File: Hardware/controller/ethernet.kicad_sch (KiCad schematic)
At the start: 21 parts

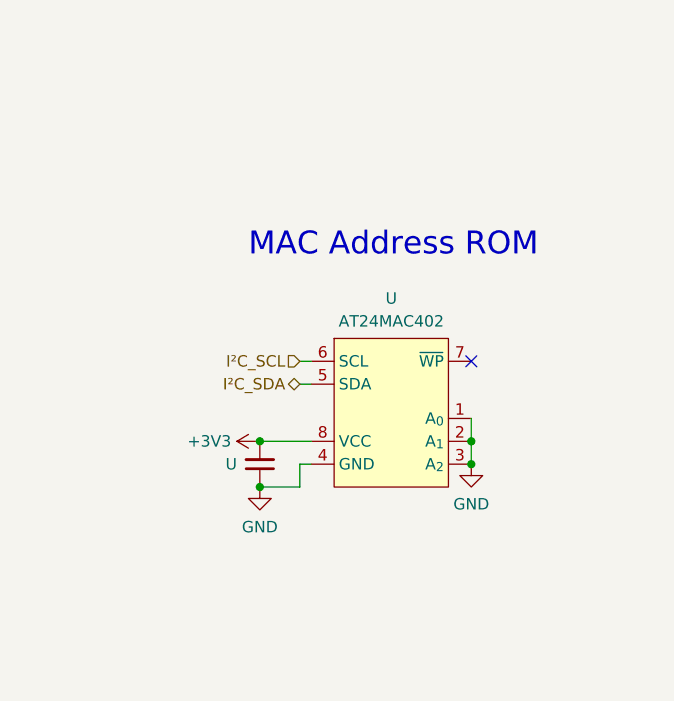
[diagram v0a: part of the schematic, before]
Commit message: Add CAN controller, power switch
- Add the schematic sheet for the CAN bus controller (MCP2515) and
  routed all of its signals, including a CAN transceiver and the
  associated SPI lines for the controller

  (tbh ideally we'd use the CAN inside the STM32 but the STM32MP151 in
  the SoM doesn't have that…)

- Added footprint for the NE1838EE mains power switch and started
  routing part of it

- Various tweaks to controller layout
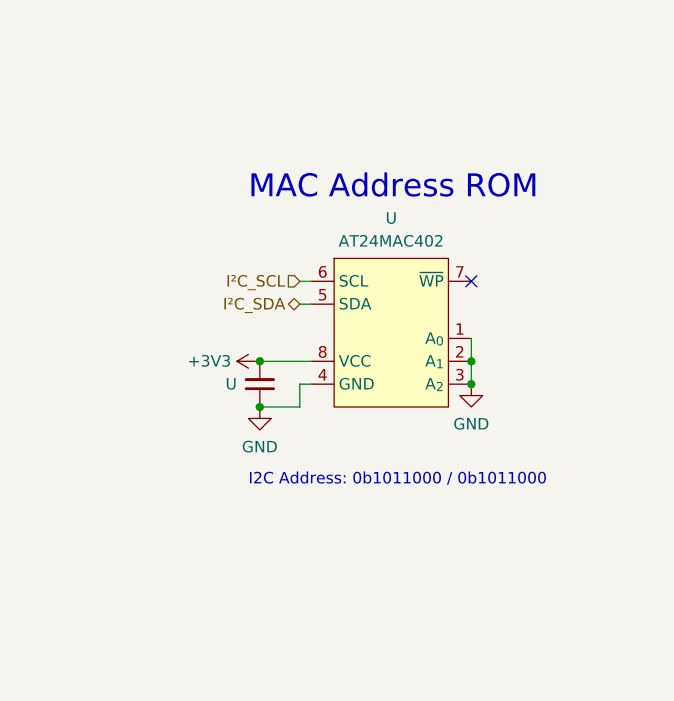
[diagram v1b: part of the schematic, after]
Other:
- note added: "I2C Address: 0b1011000 / 0b1011000"
- moved on the sheet: U

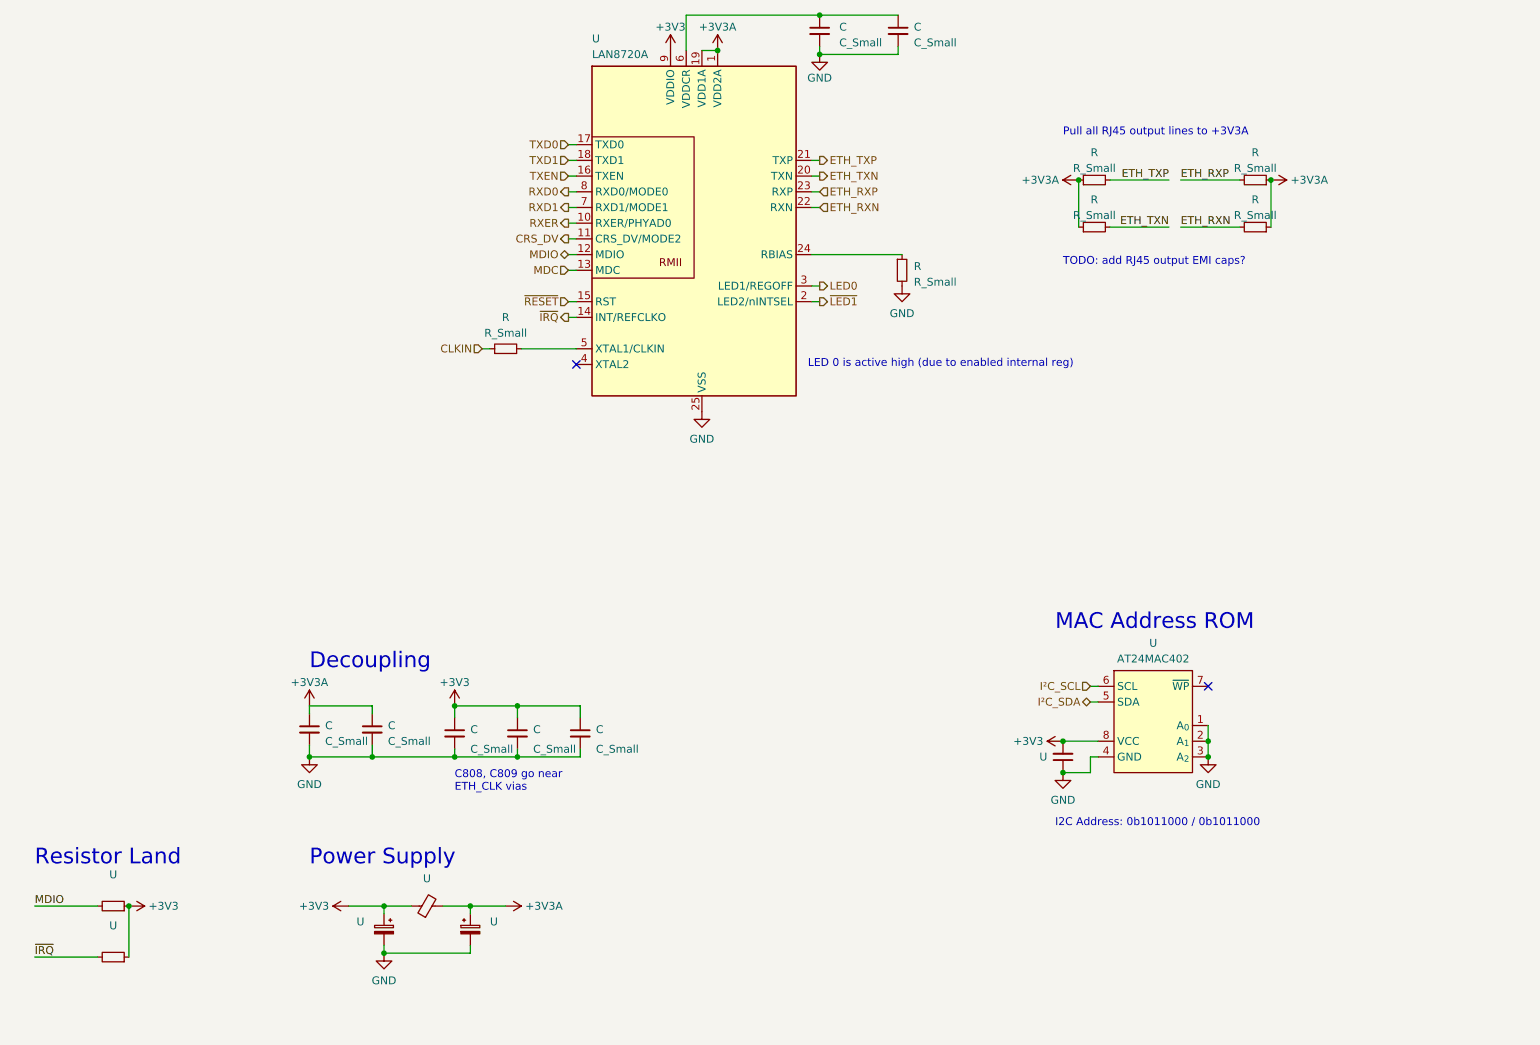
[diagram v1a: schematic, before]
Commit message: Minor Ethernet/IO tweaks
- Added (optional) EMI filter caps to Ethernet diff pairs

- Tweaked routing of the IO section slightly, and routed the GND2 plane
  (chassis ground) which connects to chassis by means of a screw
  terminal "pad" on the bottom right screw

  (Should each screw be conductive? A GND2 ring around the board?)

- Routed CPU SWD connector

- Fixed USB connector footprint to properly break out the shields in a
  way that's compatible with the KiCad USB connector symbols
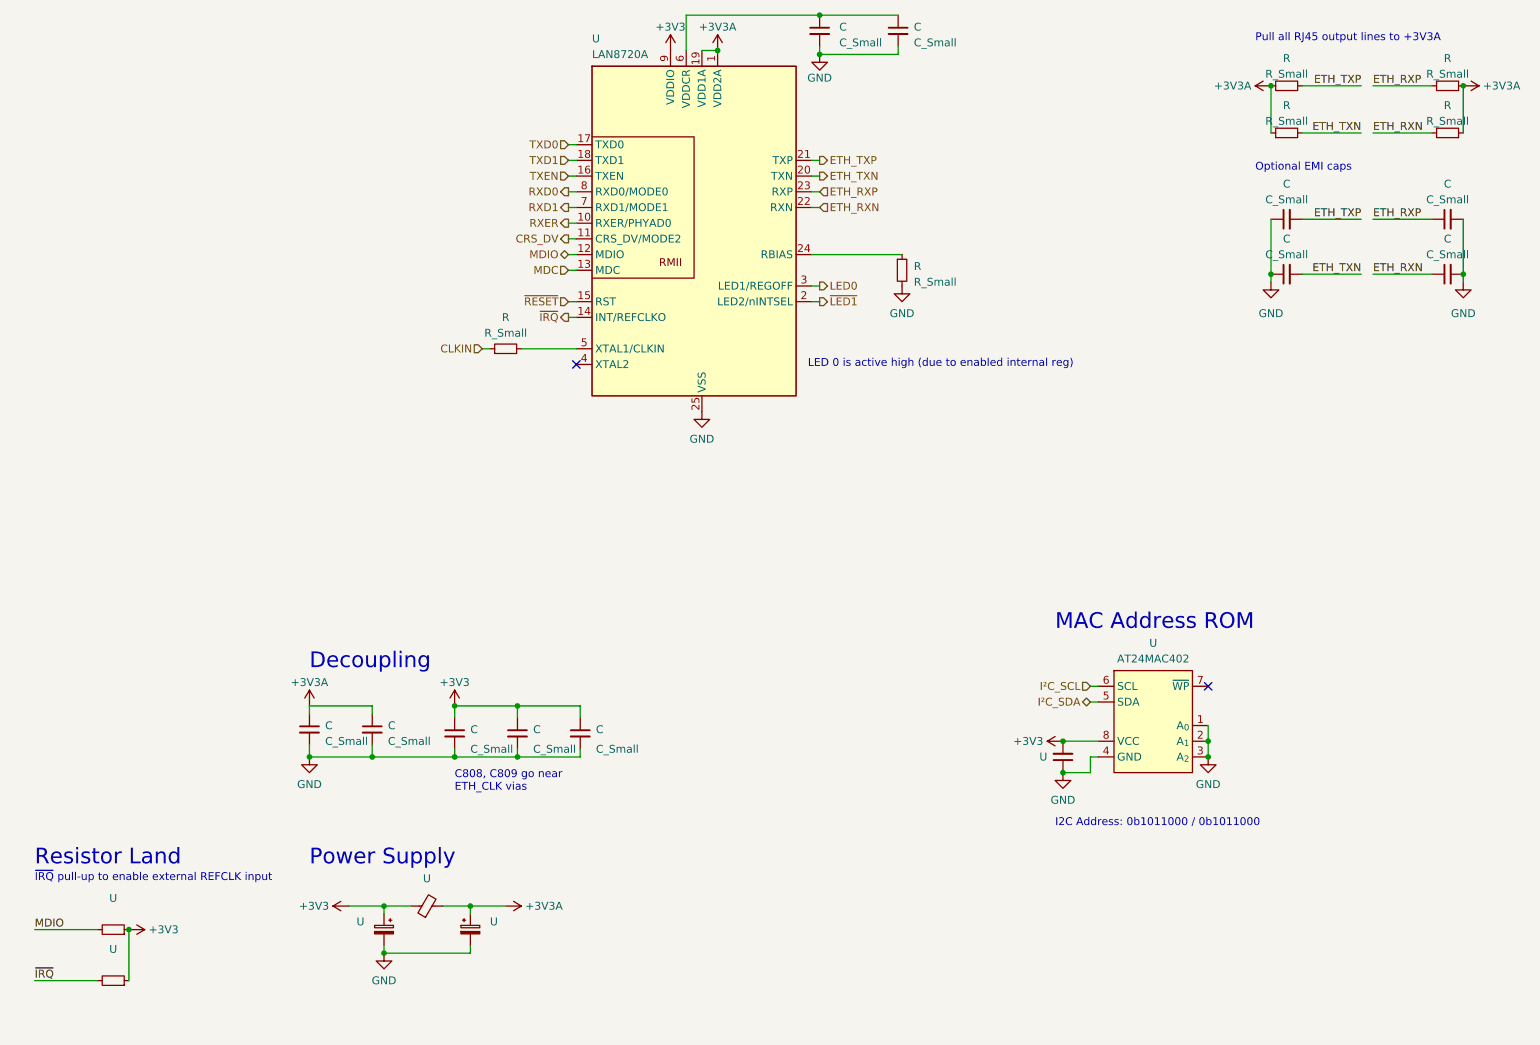
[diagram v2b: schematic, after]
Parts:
- added C (x4): C_Small, symbol Device:C_Small
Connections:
- net ETH_RXN: now also C.1
- net ETH_RXP: now also C.1
- net ETH_TXN: now also C.2
- net ETH_TXP: now also C.2
- net GND: now also C.1, C.1, C.2, C.2
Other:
- note added: "Optional EMI caps"
- note added: "~{IRQ} pull-up to enable external REFCLK input"
- note removed: "TODO: add RJ45 output EMI caps?"
- moved on the sheet: R, U

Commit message: Minor tweaks to front panel & controller for manufacture
- Create footprint for JLCPCB assembly tooling holes

- Added tooling holes to front panel board and fixed ERC errors

- Added tooling holes to controller

- Moved a few traces on controller board and fixed a few broken package
  associations

- Add pull-up on Ethernet PHY's reset line (so when the SoM boots, we're
  not making it angerey)

- Fixed order of BOOTx pins to DIP switch

- Fixed swapped USB host/device pins

- Fixed swapped ETH_TXP/ETH_TXN pair on when exiting the CPU sheet and
  connecting to the rear IO sheet (in the main sheet of the schematic)
  and the associated incorrect resistors/caps
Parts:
- added R: R_Small, symbol Device:R_Small
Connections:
- net +3V3: now also R.2
- net ~{RESET}: now also R.1
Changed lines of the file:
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@@
   (junction (at 75.565 179.07) (diameter 0) (color 0 0 0 0)
+  )
+  (junction (at 34.29 183.515) (diameter 0) (color 0 0 0 0)
   )
   (junction (at 208.915 144.78) (diameter 0) (color 0 0 0 0)
@@
     (stroke (width 0) (type default))
   )
+  (wire (pts (xy 34.29 183.515) (xy 34.29 191.135))
+    (stroke (width 0) (type default))
+  )
   (wire (pts (xy 235.585 38.735) (xy 245.11 38.735))
     (stroke (width 0) (type default))
@@
   )
   (wire (pts (xy 105.41 60.96) (xy 106.68 60.96))
+    (stroke (width 0) (type default))
+  )
+  (wire (pts (xy 19.05 191.135) (xy 29.21 191.135))
     (stroke (width 0) (type default))
   )
@@
   )
   (label "ETH_RXN" (at 235.585 46.355 0) (fields_autoplaced)
+    (effects (font (size 1.27 1.27)) (justify left bottom))
+  )
+  (label "~{RESET}" (at 19.05 191.135 0) (fields_autoplaced)
     (effects (font (size 1.27 1.27)) (justify left bottom))
   )
@@
     (pin "1")
   )
+  (symbol (lib_id "Device:R_Small") (at 31.75 191.135 90) (unit 1)
+    (in_bom yes) (on_board yes)
+    (default_instance (reference "R") (unit 1) (value "R_Small") (footprint ""))
+    (property "Reference" "R" (id 0) (at 31.75 186.69 90)
+      (effects (font (size 1.27 1.27)))
+    )
+    (property "Value" "R_Small" (id 1) (at 31.75 188.595 90)
+      (effects (font (size 1.27 1.27)))
+    )
+    (property "Footprint" "" (id 2) (at 31.75 191.135 0)
+      (effects (font (size 1.27 1.27)) hide)
+    )
+    (property "Datasheet" "~" (id 3) (at 31.75 191.135 0)
+      (effects (font (size 1.27 1.27)) hide)
+    )
+    (pin "1")
+    (pin "2")
+  )
   (symbol (lib_id "programmable-load:+3V3A") (at 95.25 171.45 270) (unit 1)

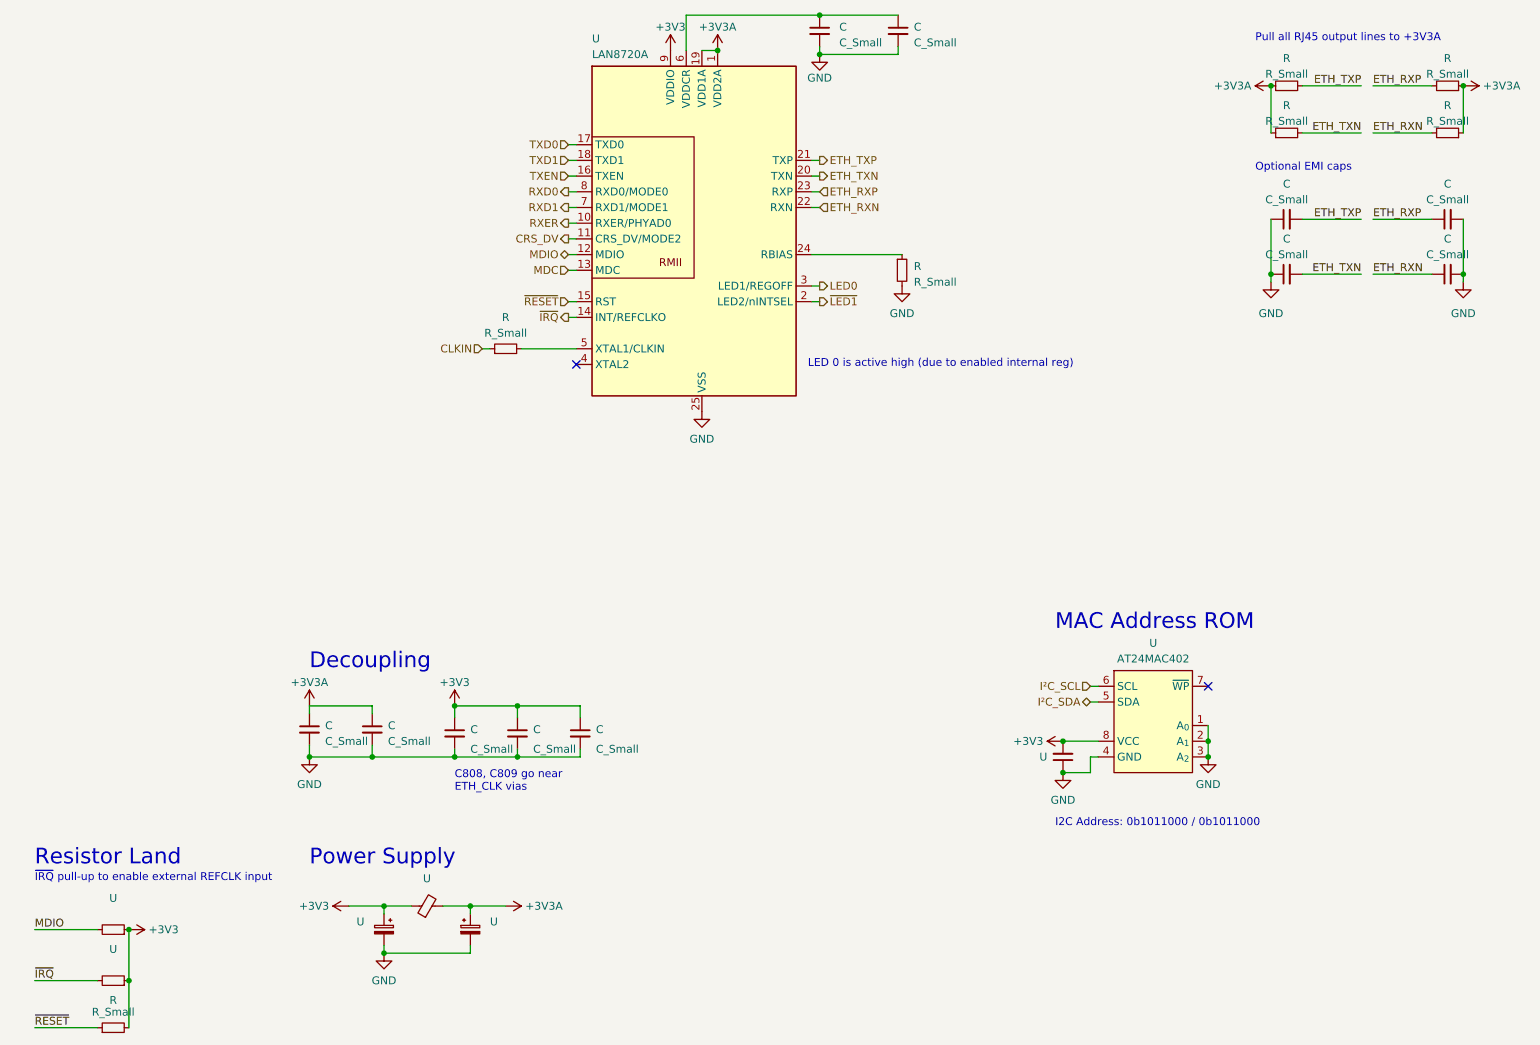
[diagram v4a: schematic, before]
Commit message: Add RMII termination resistors
- Insert resistor networks to terminate the RMII signals both at the MAC
  side and the PHY side, and re-route them with 50Ω impedance.

  Also added some additional resistors to strap pins on boot (for PHY
  address; those for MODE are using the internal ones).
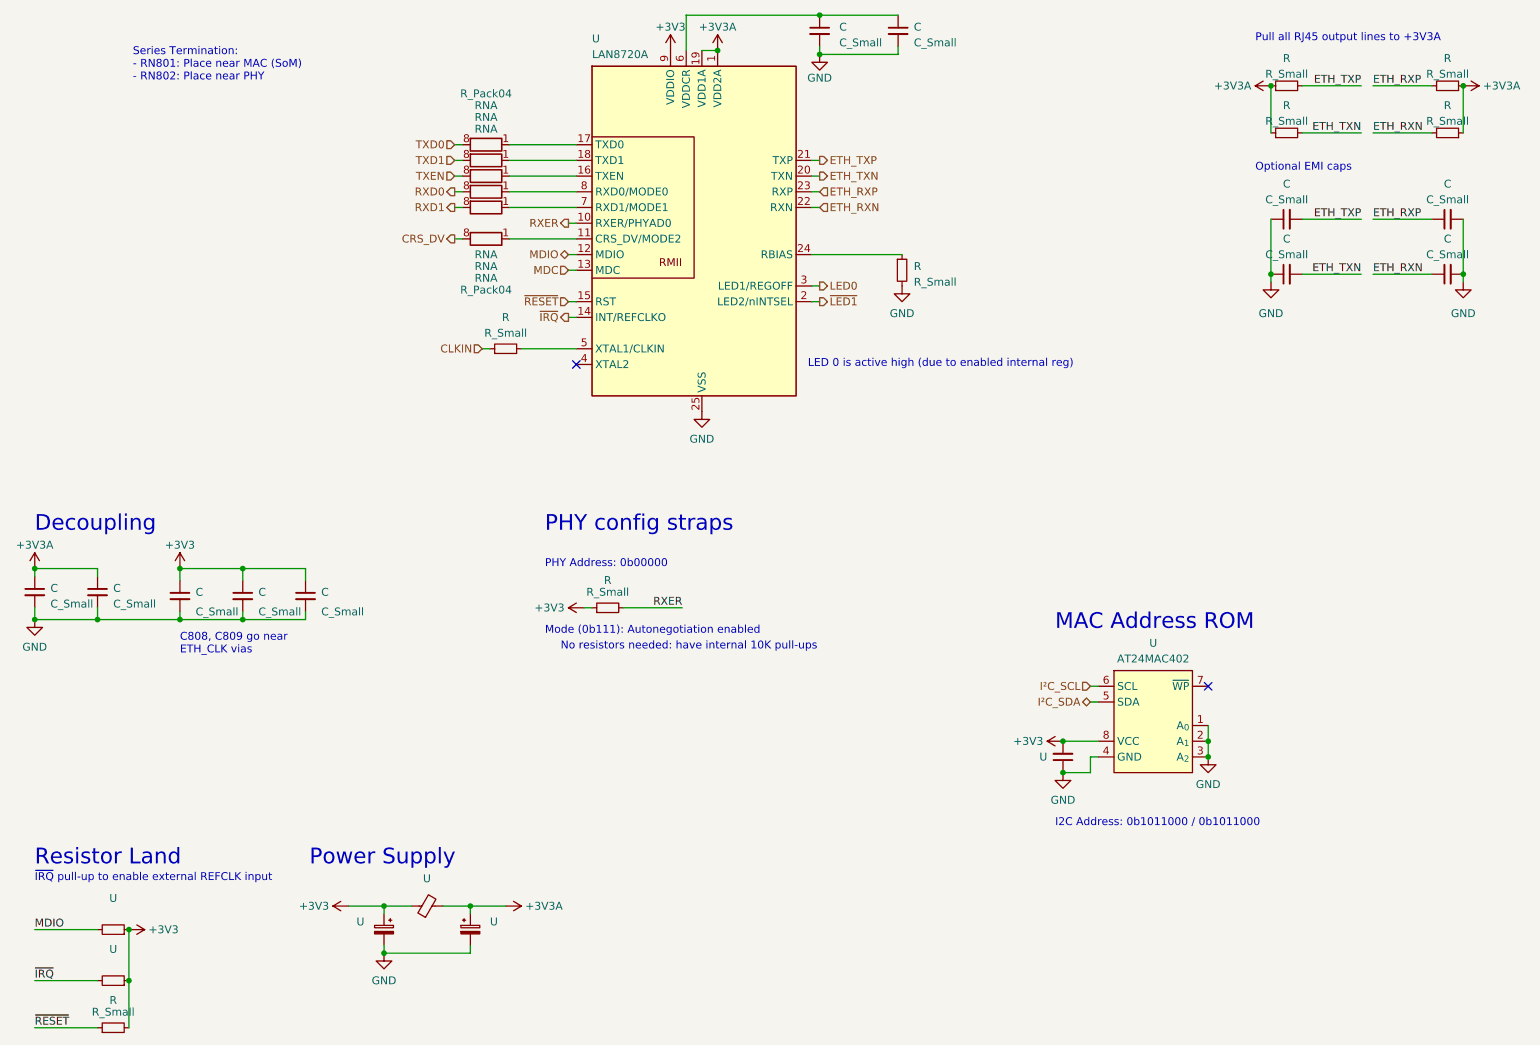
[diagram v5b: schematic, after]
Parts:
- added R: R_Small, symbol Device:R_Small
- added RN (x6): R_Pack04, symbol Device:R_Pack04_Split
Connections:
- net +3V3: now also R.1
- net CRS_DV: now also RN.8 (R1.2); no longer U.11 (CRS_DV/MODE2)
- net RXD0: now also RN.8 (R1.2); no longer U.8 (RXD0/MODE0)
- net RXD1: now also RN.8 (R1.2); no longer U.7 (RXD1/MODE1)
- net RXER: now also R.2
- net TXD0: now also RN.8 (R1.2); no longer U.17 (TXD0)
- net TXD1: now also RN.8 (R1.2); no longer U.18 (TXD1)
- net TXEN: now also RN.8 (R1.2); no longer U.16 (TXEN)
- new net: RN.1 (R1.1), U.11 (CRS_DV/MODE2)
- new net: RN.1 (R1.1), U.16 (TXEN)
- new net: RN.1 (R1.1), U.17 (TXD0)
- new net: RN.1 (R1.1), U.18 (TXD1)
- new net: RN.1 (R1.1), U.7 (RXD1/MODE1)
- new net: RN.1 (R1.1), U.8 (RXD0/MODE0)
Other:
- note added: "Mode (0b111): Autonegotiation enabled"
- note added: "No resistors needed: have internal 10K pull-ups"
- note added: "PHY Address: 0b00000"
- note added: "PHY config straps"
- note added: "Series Termination: - RN801: Place near MAC (SoM) - RN802: Place near PHY"
- moved on the sheet: C
